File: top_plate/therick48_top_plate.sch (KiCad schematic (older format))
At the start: 54 parts, among them U1 HOLE, U10 HOLE, U11 HOLE, U12 HOLE, U13 HOLE, U14 HOLE, U15 HOLE, U16 HOLE, U17 HOLE, U18 HOLE, U19 HOLE, U2 HOLE, U20 HOLE, U21 HOLE, U22 HOLE, U23 HOLE, U24 HOLE, U25 HOLE, U26 HOLE, U27 HOLE, U28 HOLE, U29 HOLE, U3 HOLE, U30 HOLE, U31 HOLE, U32 HOLE, U33 HOLE, U34 HOLE, U35 HOLE, U36 HOLE, U37 HOLE, U38 HOLE, U39 HOLE, U4 HOLE, U40 HOLE, U41 HOLE, U42 HOLE, U43 HOLE, U44 HOLE, U45 HOLE, U46 HOLE, U47 HOLE, U48 HOLE, U5 HOLE, U6 HOLE, U7 HOLE, U8 HOLE, U9 HOLE

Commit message: Updated mounting holes
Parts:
- H1, H2, H3, H4, H5, H6: footprint random-keyboard-parts:plate_hole_4mm_tht -> random-keyboard-parts:Generic-Mounthole
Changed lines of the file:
@@
 EESchema Schematic File Version 4
-LIBS:therick64BA_19mm_top_plate-cache
+LIBS:therick48_top_plate-cache
 EELAYER 29 0
 EELAYER END
@@
 F 0 "H2" H 4550 5596 50  0000 L CNN
 F 1 "MountingHole" H 4550 5505 50  0000 L CNN
-F 2 "random-keyboard-parts:plate_hole_4mm_tht" H 4450 5550 50  0001 C CNN
+F 2 "random-keyboard-parts:Generic-Mounthole" H 4450 5550 50  0001 C CNN
 F 3 "~" H 4450 5550 50  0001 C CNN
 	1    4450 5550
@@
 F 0 "H1" H 4550 5396 50  0000 L CNN
 F 1 "MountingHole" H 4550 5305 50  0000 L CNN
-F 2 "random-keyboard-parts:plate_hole_4mm_tht" H 4450 5350 50  0001 C CNN
+F 2 "random-keyboard-parts:Generic-Mounthole" H 4450 5350 50  0001 C CNN
 F 3 "~" H 4450 5350 50  0001 C CNN
 	1    4450 5350
@@
 F 0 "H3" H 4550 5796 50  0000 L CNN
 F 1 "MountingHole" H 4550 5705 50  0000 L CNN
-F 2 "random-keyboard-parts:plate_hole_4mm_tht" H 4450 5750 50  0001 C CNN
+F 2 "random-keyboard-parts:Generic-Mounthole" H 4450 5750 50  0001 C CNN
 F 3 "~" H 4450 5750 50  0001 C CNN
 	1    4450 5750
@@
 F 0 "H4" H 4550 5996 50  0000 L CNN
 F 1 "MountingHole" H 4550 5905 50  0000 L CNN
-F 2 "random-keyboard-parts:plate_hole_4mm_tht" H 4450 5950 50  0001 C CNN
+F 2 "random-keyboard-parts:Generic-Mounthole" H 4450 5950 50  0001 C CNN
 F 3 "~" H 4450 5950 50  0001 C CNN
 	1    4450 5950
@@
 F 0 "H5" H 4550 6196 50  0000 L CNN
 F 1 "MountingHole" H 4550 6105 50  0000 L CNN
-F 2 "random-keyboard-parts:plate_hole_4mm_tht" H 4450 6150 50  0001 C CNN
+F 2 "random-keyboard-parts:Generic-Mounthole" H 4450 6150 50  0001 C CNN
 F 3 "~" H 4450 6150 50  0001 C CNN
 	1    4450 6150
@@
 F 0 "H6" H 4550 6396 50  0000 L CNN
 F 1 "MountingHole" H 4550 6305 50  0000 L CNN
-F 2 "random-keyboard-parts:plate_hole_4mm_tht" H 4450 6350 50  0001 C CNN
+F 2 "random-keyboard-parts:Generic-Mounthole" H 4450 6350 50  0001 C CNN
 F 3 "~" H 4450 6350 50  0001 C CNN
 	1    4450 6350

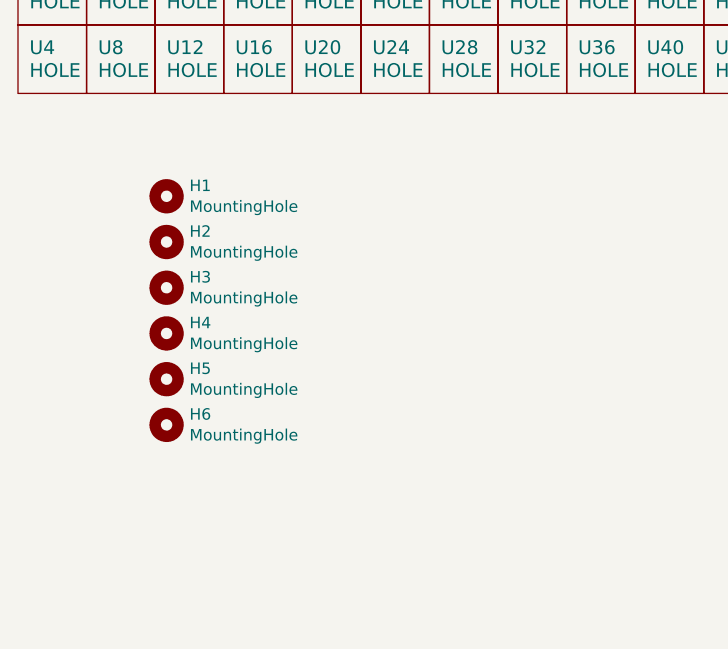
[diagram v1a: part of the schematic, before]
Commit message: Added more mounting holes
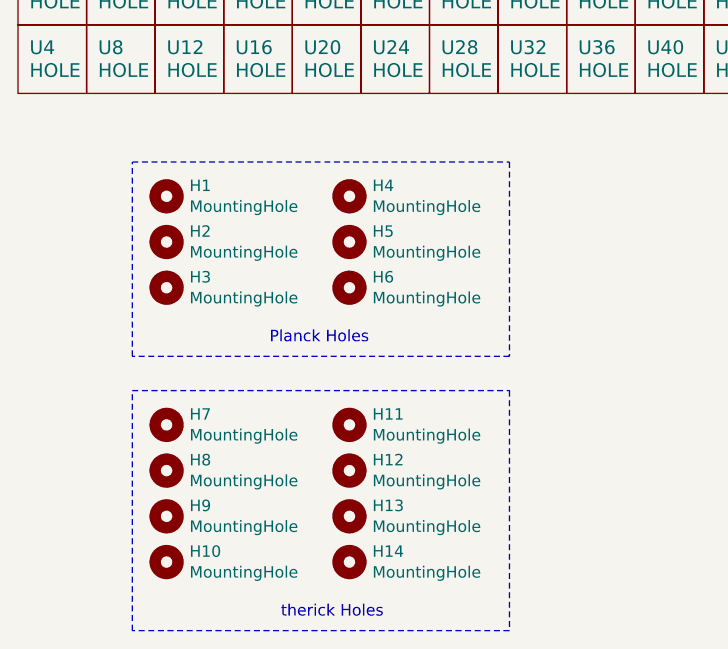
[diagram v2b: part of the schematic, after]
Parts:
- added H10, H11, H12, H13, H14, H7, H8, H9: MountingHole, random-keyboard-parts:Generic-Mounthole, symbol Mechanical:MountingHole
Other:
- note added: "Planck Holes"
- note added: "therick Holes"
- moved on the sheet: H4, H5, H6
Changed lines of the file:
@@
 L Mechanical:MountingHole H4
 U 1 1 5DAFCFC0
-P 4450 5950
-F 0 "H4" H 4550 5996 50  0000 L CNN
-F 1 "MountingHole" H 4550 5905 50  0000 L CNN
-F 2 "random-keyboard-parts:Generic-Mounthole" H 4450 5950 50  0001 C CNN
-F 3 "~" H 4450 5950 50  0001 C CNN
-	1    4450 5950
+P 5250 5350
+F 0 "H4" H 5350 5396 50  0000 L CNN
+F 1 "MountingHole" H 5350 5305 50  0000 L CNN
+F 2 "random-keyboard-parts:Generic-Mounthole" H 5250 5350 50  0001 C CNN
+F 3 "~" H 5250 5350 50  0001 C CNN
+	1    5250 5350
 	1    0    0    -1
 $EndComp
@@
 L Mechanical:MountingHole H5
 U 1 1 5DAFD908
-P 4450 6150
-F 0 "H5" H 4550 6196 50  0000 L CNN
-F 1 "MountingHole" H 4550 6105 50  0000 L CNN
-F 2 "random-keyboard-parts:Generic-Mounthole" H 4450 6150 50  0001 C CNN
-F 3 "~" H 4450 6150 50  0001 C CNN
-	1    4450 6150
+P 5250 5550
+F 0 "H5" H 5350 5596 50  0000 L CNN
+F 1 "MountingHole" H 5350 5505 50  0000 L CNN
+F 2 "random-keyboard-parts:Generic-Mounthole" H 5250 5550 50  0001 C CNN
+F 3 "~" H 5250 5550 50  0001 C CNN
+	1    5250 5550
 	1    0    0    -1
 $EndComp
@@
 L Mechanical:MountingHole H6
 U 1 1 5DAFE1B7
-P 4450 6350
-F 0 "H6" H 4550 6396 50  0000 L CNN
-F 1 "MountingHole" H 4550 6305 50  0000 L CNN
-F 2 "random-keyboard-parts:Generic-Mounthole" H 4450 6350 50  0001 C CNN
-F 3 "~" H 4450 6350 50  0001 C CNN
-	1    4450 6350
+P 5250 5750
+F 0 "H6" H 5350 5796 50  0000 L CNN
+F 1 "MountingHole" H 5350 5705 50  0000 L CNN
+F 2 "random-keyboard-parts:Generic-Mounthole" H 5250 5750 50  0001 C CNN
+F 3 "~" H 5250 5750 50  0001 C CNN
+	1    5250 5750
 	1    0    0    -1
 $EndComp
@@
 	1    0    0    -1
 $EndComp
+$Comp
+L Mechanical:MountingHole H8
+U 1 1 5ED3E76C
+P 4450 6550
+F 0 "H8" H 4550 6596 50  0000 L CNN
+F 1 "MountingHole" H 4550 6505 50  0000 L CNN
+F 2 "random-keyboard-parts:Generic-Mounthole" H 4450 6550 50  0001 C CNN
+F 3 "~" H 4450 6550 50  0001 C CNN
+	1    4450 6550
+	1    0    0    -1
+$EndComp
+$Comp
+L Mechanical:MountingHole H7
+U 1 1 5ED3E772
+P 4450 6350
+F 0 "H7" H 4550 6396 50  0000 L CNN
+F 1 "MountingHole" H 4550 6305 50  0000 L CNN
+F 2 "random-keyboard-parts:Generic-Mounthole" H 4450 6350 50  0001 C CNN
+F 3 "~" H 4450 6350 50  0001 C CNN
+	1    4450 6350
+	1    0    0    -1
+$EndComp
+$Comp
+L Mechanical:MountingHole H9
+U 1 1 5ED3E778
+P 4450 6750
+F 0 "H9" H 4550 6796 50  0000 L CNN
+F 1 "MountingHole" H 4550 6705 50  0000 L CNN
+F 2 "random-keyboard-parts:Generic-Mounthole" H 4450 6750 50  0001 C CNN
+F 3 "~" H 4450 6750 50  0001 C CNN
+	1    4450 6750
+	1    0    0    -1
+$EndComp
+$Comp
+L Mechanical:MountingHole H11
+U 1 1 5ED3E77E
+P 5250 6350
+F 0 "H11" H 5350 6396 50  0000 L CNN
+F 1 "MountingHole" H 5350 6305 50  0000 L CNN
+F 2 "random-keyboard-parts:Generic-Mounthole" H 5250 6350 50  0001 C CNN
+F 3 "~" H 5250 6350 50  0001 C CNN
+	1    5250 6350
+	1    0    0    -1
+$EndComp
+$Comp
+L Mechanical:MountingHole H12
+U 1 1 5ED3E784
+P 5250 6550
+F 0 "H12" H 5350 6596 50  0000 L CNN
+F 1 "MountingHole" H 5350 6505 50  0000 L CNN
+F 2 "random-keyboard-parts:Generic-Mounthole" H 5250 6550 50  0001 C CNN
+F 3 "~" H 5250 6550 50  0001 C CNN
+	1    5250 6550
+	1    0    0    -1
+$EndComp
+$Comp
+L Mechanical:MountingHole H13
+U 1 1 5ED3E78A
+P 5250 6750
+F 0 "H13" H 5350 6796 50  0000 L CNN
+F 1 "MountingHole" H 5350 6705 50  0000 L CNN
+F 2 "random-keyboard-parts:Generic-Mounthole" H 5250 6750 50  0001 C CNN
+F 3 "~" H 5250 6750 50  0001 C CNN
+	1    5250 6750
+	1    0    0    -1
+$EndComp
+$Comp
+L Mechanical:MountingHole H10
+U 1 1 5ED3ED7A
+P 4450 6950
+F 0 "H10" H 4550 6996 50  0000 L CNN
+F 1 "MountingHole" H 4550 6905 50  0000 L CNN
+F 2 "random-keyboard-parts:Generic-Mounthole" H 4450 6950 50  0001 C CNN
+F 3 "~" H 4450 6950 50  0001 C CNN
+	1    4450 6950
+	1    0    0    -1
+$EndComp
+$Comp
+L Mechanical:MountingHole H14
+U 1 1 5ED3ED80
+P 5250 6950
+F 0 "H14" H 5350 6996 50  0000 L CNN
+F 1 "MountingHole" H 5350 6905 50  0000 L CNN
+F 2 "random-keyboard-parts:Generic-Mounthole" H 5250 6950 50  0001 C CNN
+F 3 "~" H 5250 6950 50  0001 C CNN
+	1    5250 6950
+	1    0    0    -1
+$EndComp
+Text Notes 4900 6000 0    50   ~ 0
+Planck Holes
+Text Notes 4950 7200 0    50   ~ 0
+therick Holes
+Wire Notes Line
+	4300 5200 5950 5200
+Wire Notes Line
+	5950 5200 5950 6050
+Wire Notes Line
+	5950 6050 4300 6050
+Wire Notes Line
+	4300 6050 4300 5200
+Wire Notes Line
+	4300 6200 5950 6200
+Wire Notes Line
+	5950 6200 5950 7250
+Wire Notes Line
+	5950 7250 4300 7250
+Wire Notes Line
+	4300 7250 4300 6200
 $EndSCHEMATC

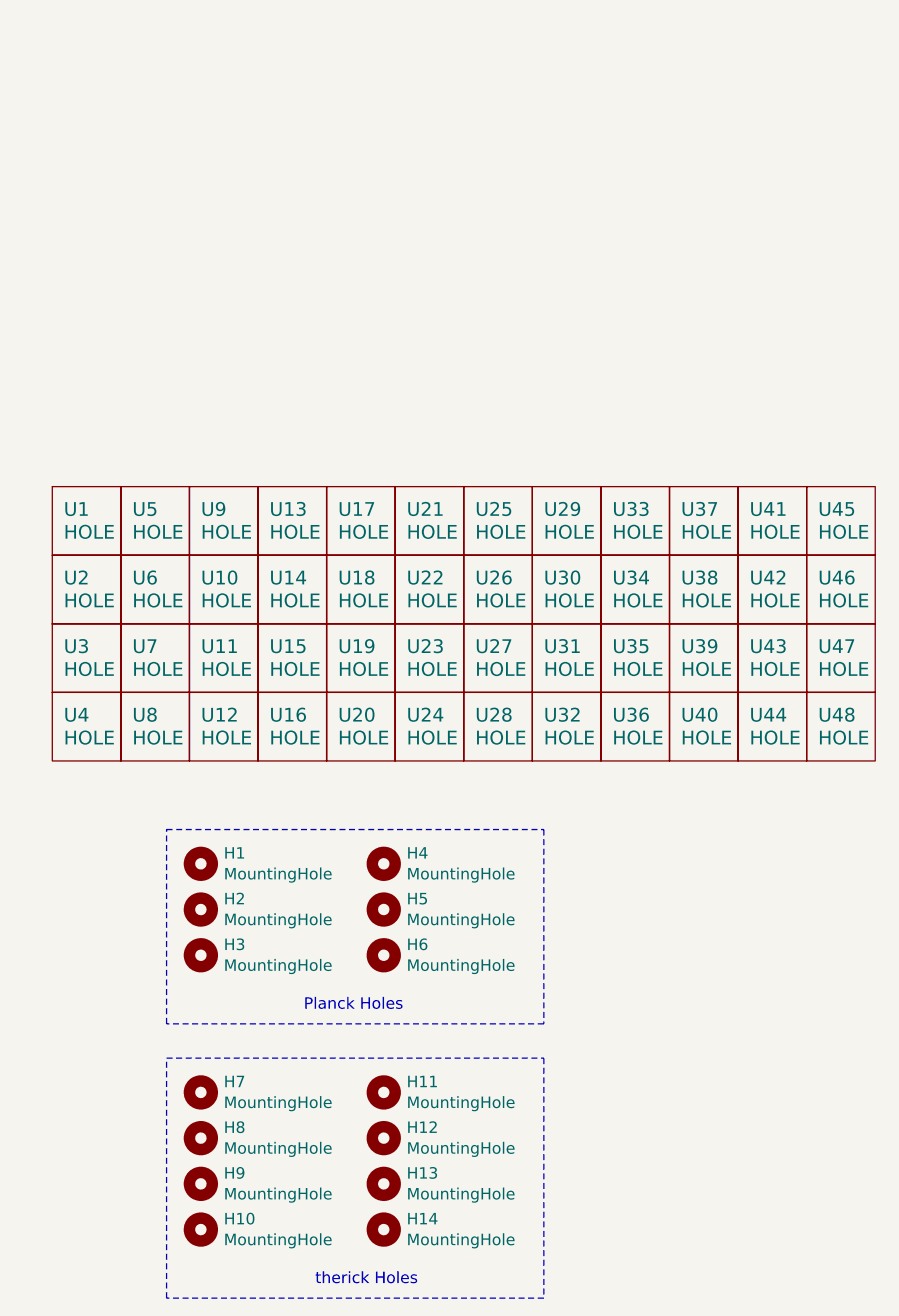
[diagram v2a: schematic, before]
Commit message: Move mounting holes to PCB
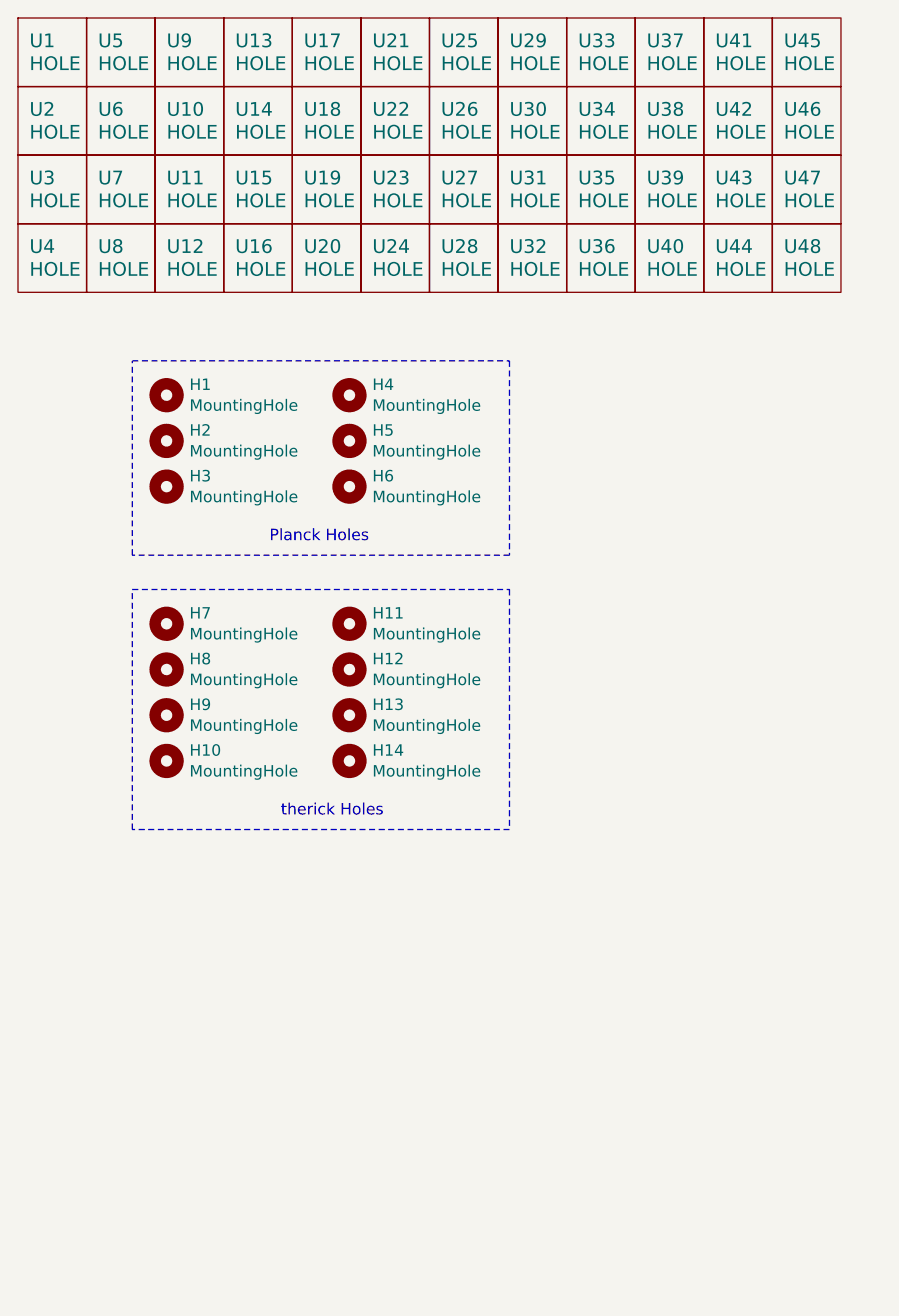
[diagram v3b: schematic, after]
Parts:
- H1, H10, H11, H12, H13, H14, H2, H3, H4, H5, H6, H7, H8, H9: footprint random-keyboard-parts:Generic-Mounthole -> random-keyboard-parts:plate_hole_4mm_tht
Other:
- moved on the sheet: H1, H10, H11, H12, H13, H14, H2, H3, H4, H5, H6, H7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
